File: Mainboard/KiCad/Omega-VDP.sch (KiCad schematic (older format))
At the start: 63 parts, among them J2 Composite, J4 S-VIDEO, J5 RGB, Q2 PN2222A, U10 D41464, U11 D41464, U3 V9938, U39 74AHCT32, U43 74HCT04, U47 CXA1645, U8 D41464, U9 D41464, Y1 21.477270MHz, Y3 4.433618MHz

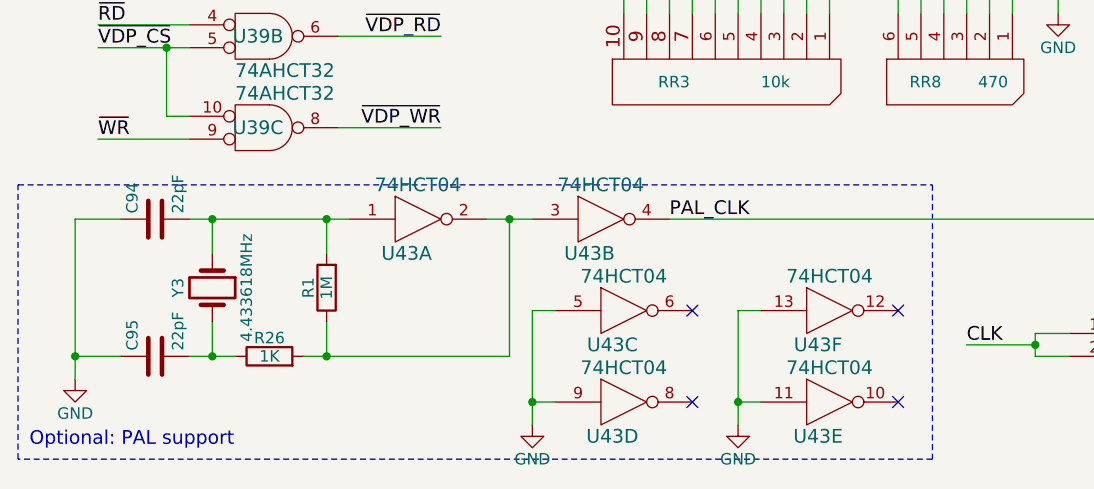
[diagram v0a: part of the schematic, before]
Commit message: Mainboard: Update to version 1.0
Signed-off-by: Sergey Kiselev <skiselev@gmail.com>
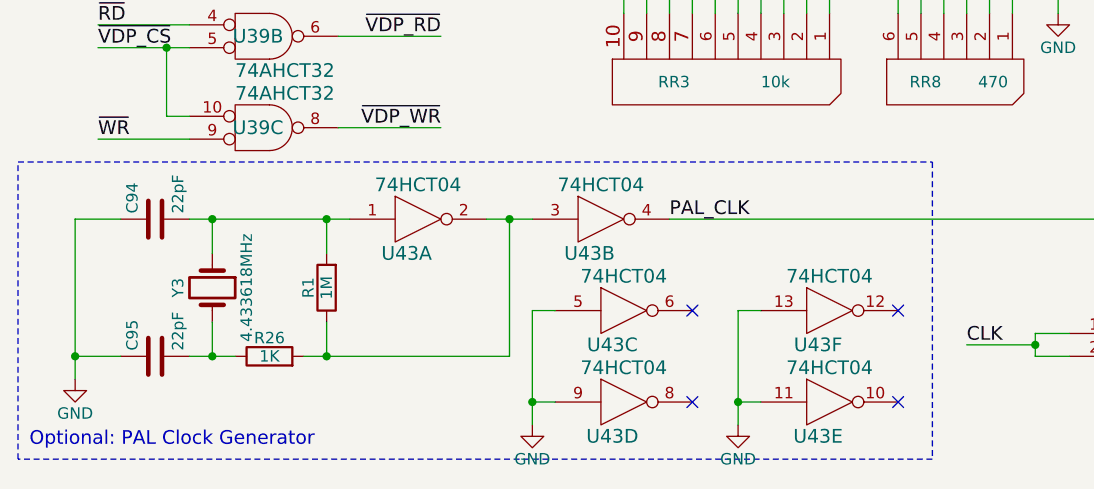
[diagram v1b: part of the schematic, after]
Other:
- note added: "Optional: PAL Clock Generator"
- note removed: "Optional: PAL support"
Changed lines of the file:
@@
 Connection ~ 5000 7250
 Text Notes 600  7700 0    60   ~ 0
-Optional: PAL support
+Optional: PAL Clock Generator
 $Comp
 L Transistor_BJT:PN2222A Q2
@@
 SYNC
 Wire Notes Line
-	4550 6550 4550 7750
-Wire Notes Line
-	550  7750 550  6550
+	4550 6450 4550 7750
+Wire Notes Line
+	550  7750 550  6450
 $Comp
 L my_components:74LS04 U43
@@
 	4550 7750 550  7750
 Wire Notes Line
-	550  6550 4550 6550
+	550  6450 4550 6450
 Wire Wire Line
 	2900 7100 2800 7100

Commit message: Mainboard: Fix the issues discovered so far
Signed-off-by: Sergey Kiselev <skiselev@gmail.com>
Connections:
- net CLK: now also U39.4, U39.5; no longer U39.1, U39.2
- net ~RD: now also U39.1; no longer U39.4
- net ~VDP_CS: now also U39.13, U39.2; no longer U39.10, U39.5
- net ~VDP_RD: now also U39.3; no longer U39.6
- net ~VDP_WR: now also U39.11; no longer U39.8
- net ~WR: now also U39.12; no longer U39.9
- net at JP5.1: now also U39.6; no longer U39.3
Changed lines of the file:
@@
 $Comp
 L my_components:74LS32 U39
-U 3 2 5A4E2C23
+U 4 2 5A4E2C23
 P 1600 6300
 F 0 "U39" H 1600 6300 60  0000 C CNN
@@
 F 2 "My_Components:IC_DIP14_300" H 1600 6300 60  0001 C CNN
 F 3 "" H 1600 6300 60  0000 C CNN
-	3    1600 6300
+	4    1600 6300
 	1    0    0    1
 $EndComp
 $Comp
 L my_components:74LS32 U39
-U 2 2 5A4E3114
+U 1 2 5A4E3114
 P 1600 5900
 F 0 "U39" H 1600 5900 60  0000 C CNN
@@
 F 2 "My_Components:IC_DIP14_300" H 1600 5900 60  0001 C CNN
 F 3 "" H 1600 5900 60  0000 C CNN
-	2    1600 5900
+	1    1600 5900
 	1    0    0    -1
 $EndComp
@@
 $Comp
 L my_components:74LS32 U39
-U 1 1 5C142396
+U 2 1 5C142396
 P 5450 7250
 F 0 "U39" H 5450 7250 60  0000 C CNN
@@
 F 2 "My_Components:IC_DIP14_300" H 5450 7250 60  0001 C CNN
 F 3 "" H 5450 7250 60  0000 C CNN
-	1    5450 7250
-	1    0    0    -1
-$EndComp
+	2    5450 7250
+	1    0    0    -1
+$EndComp

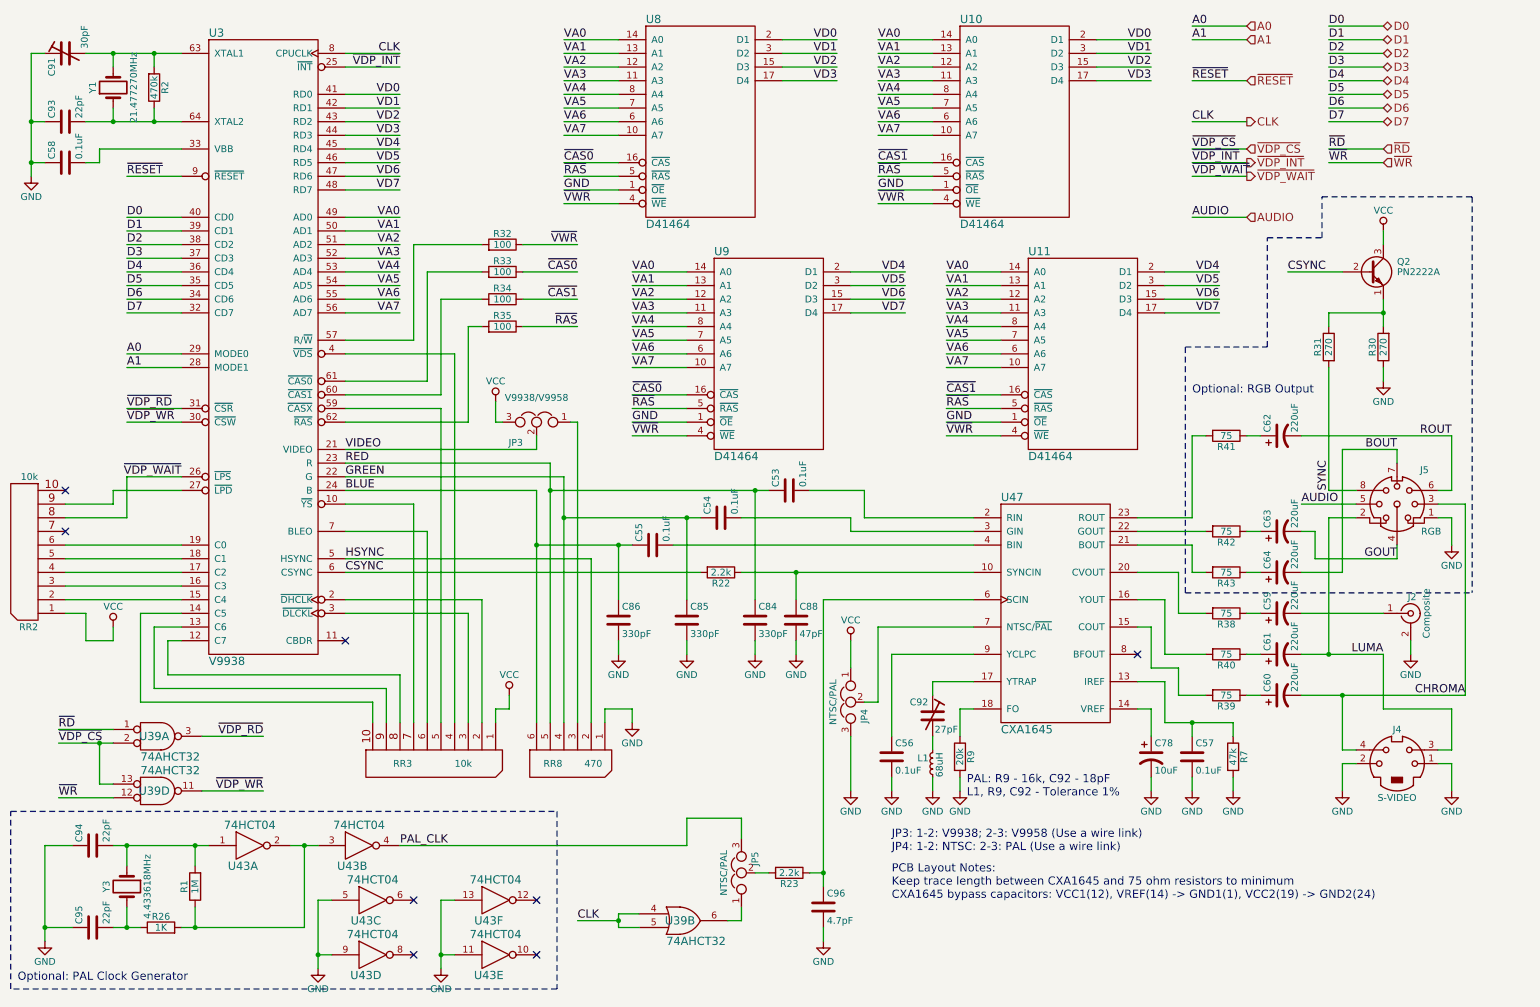
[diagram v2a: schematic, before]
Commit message: Mainboard: Fixed schematic and PCB for v1.1
Signed-off-by: Sergey Kiselev <skiselev@gmail.com>
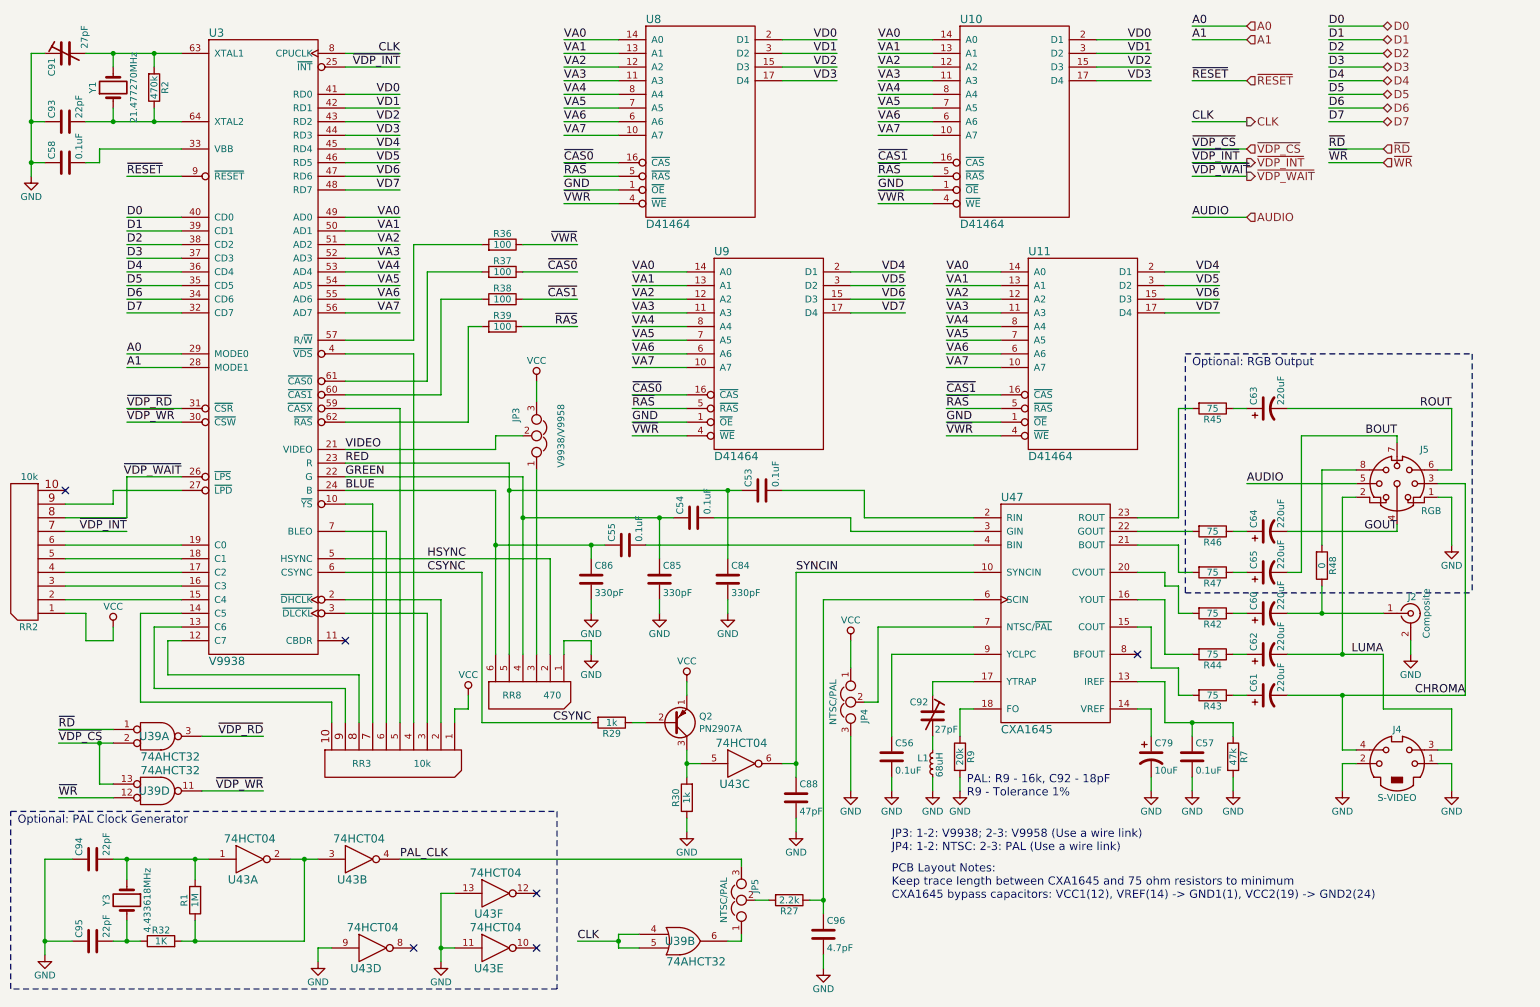
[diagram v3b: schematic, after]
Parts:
- removed Q2: PN2222A, My_Components:Transistor_TO92_EBC_254, symbol Transistor_BJT:PN2222A
- added Q2: PN2907A, My_Components:Transistor_TO92_EBC_254, symbol Transistor_BJT:2N3906
- C91: value 30pF -> 27pF
- R29: renamed from R22; value 2.2k -> 1k
- R30: value 270 -> 1k
- R48: renamed from R31; value 270 -> 0
- renumbered C59 to C60, C60 to C61, C61 to C62, C62 to C63, C63 to C64, C64 to C65, C78 to C79, R23 to R27, R26 to R32, R32 to R36, R33 to R37, R34 to R38, R35 to R39, R38 to R42, R39 to R43, R40 to R44, R41 to R45, R42 to R46, R43 to R47
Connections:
- net GND: no longer U43.5
- net VCC: now also Q2.1 (E)
- net ~VDP_INT: now also RR2.7
- net at C60.2, J2.1 (In): now also R48.1
- net SYNCIN: now reaches C88.1, U47.10 (SYNCIN)
- net SYNCIN: now also U43.6; no longer R29.1
- net at R30.2: now also U43.5, Q2.3 (C); no longer R48.1
- net SYNC: no longer names the net of J5.8, R48.2
- new net: Q2.2 (B), R29.1
- no-connect marks 8 -> 6
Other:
- note added: "PAL: R9 - 16k, C92 - 18pF\nR9 - Tolerance 1%"
- note removed: "PAL: R9 - 16k, C92 - 18pF\nL1, R9, C92 - Tolerance 1%"
- moved on the sheet: C53, C54, C55, C60, C61, C62, C63, C64, C65, C84, C85, C86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

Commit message: Mainboard: Replace RGB and Cassette connectors with DIN8
Signed-off-by: Sergey Kiselev <skiselev@gmail.com>
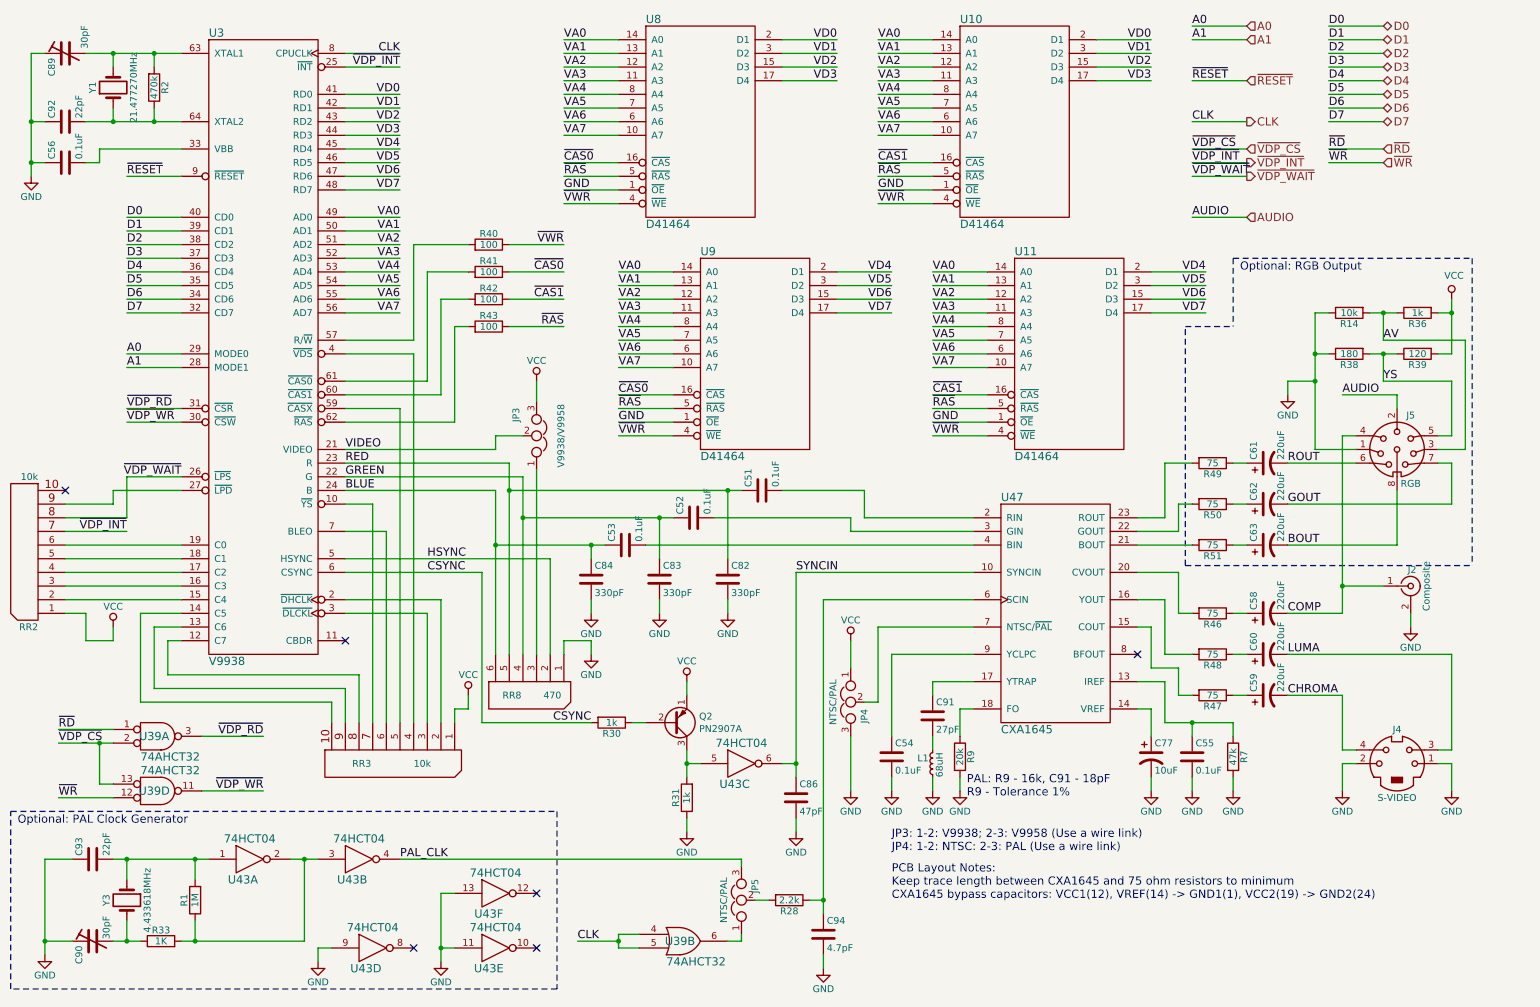
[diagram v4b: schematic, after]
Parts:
- removed J5: RGB, My_Components:Conn_Mini_DIN_8pin, symbol Connector:Mini-DIN-8
- added J5: RGB, My_Components:Conn_DIN_8pin, symbol Connector:DIN-8
- added R14: 10k, My_Components:Res_762, symbol Device:R
- added R38: 180, My_Components:Res_762, symbol Device:R
- added R39: 120, My_Components:Res_762, symbol Device:R
- C89: renamed from C91; value 27pF -> 30pF
- C90: renamed from C92; value 27pF -> 30pF
- C91: renamed from C95; value 22pF -> 27pF
- R36: renamed from R48; value 0 -> 1k
- renumbered C53 to C51, C54 to C52, C55 to C53, C56 to C54, C57 to C55, C58 to C56, C60 to C58, C61 to C59, C62 to C60, C63 to C61, C64 to C62, C65 to C63, C79 to C77, C84 to C82, C85 to C83, C86 to C84, C88 to C86, C93 to C92, C94 to C93, C96 to C94, R27 to R28, R29 to R30, R30 to R31, R32 to R33, R36 to R40, R37 to R41, R38 to R42, R39 to R43, R42 to R46, R43 to R47, R44 to R48, R45 to R49, R46 to R50, R47 to R51
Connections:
- net AUDIO: now also J5.2
- net BOUT: now also J5.8
- net GND: now also C90.1, J5.1, R14.1, R38.1; no longer C91.1
- net GOUT: now also J5.7
- net ROUT: now also J5.6
- net VCC: now also R36.2, R39.2
- net COMP: now reaches C58.2, J2.1 (In)
- net COMP: now also J5.4; no longer R36.1
- net at U47.17 (YTRAP): now also C91.1; no longer C90.1
- net at L1.1: now also C91.2; no longer C90.2
- net at R33.1, Y3.2: now also C90.2; no longer C91.2
- new net AV: J5.3, R14.2, R36.1
- new net YS: J5.5, R38.2, R39.1
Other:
- note added: "PAL: R9 - 16k, C91 - 18pF\nR9 - Tolerance 1%"
- note removed: "PAL: R9 - 16k, C92 - 18pF\nR9 - Tolerance 1%"
- moved on the sheet: C61, C62, C63, C90, C91, J2, R36, R40, R41, R42, R43, R49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
